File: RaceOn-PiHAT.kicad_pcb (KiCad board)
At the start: 2 copper layers, 65 x 56.5 mm, 76 parts, among them IC1 MIC29302WU, IC10 SN74LVC2G07, IC2 NCP5901B, IC3 NCP5901B, IC4 BD48K60G, IC5 LMR14030, IC6 MPU-9250, IC7 SN74LVC2G07, IC8 SN74LVC2G07, IC9 SN74LVC2G07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

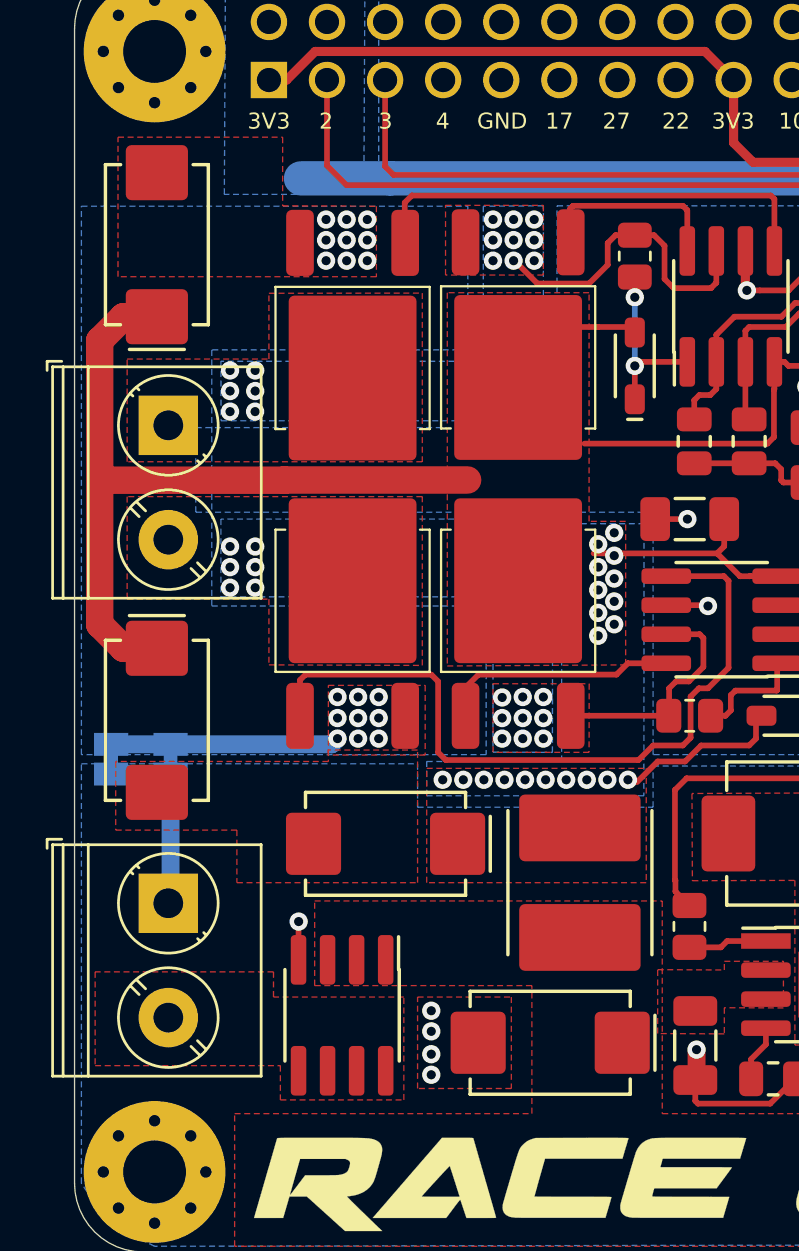
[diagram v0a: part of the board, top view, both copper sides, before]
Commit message: Remove EMI filter, replace low ESR caps with ceramic
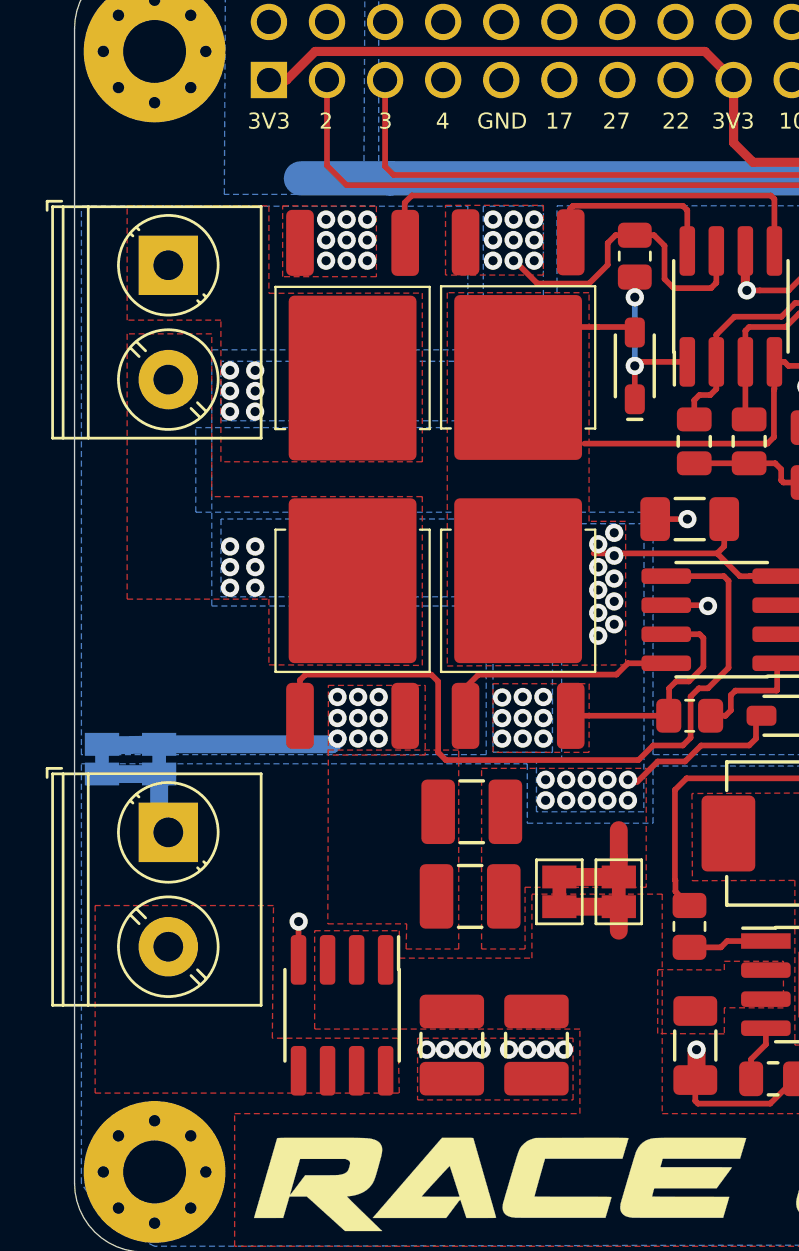
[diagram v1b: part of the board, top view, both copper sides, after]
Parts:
- removed L2: 1uH, Race On:INDM600X600X450L155X490M
- added JP5: SolderJumper_2_Bridged, Jumper:SolderJumper-2_P1.3mm_Bridged_Pad1.0x1.5mm, B.Cu at (120.7, 96.7)
- added JP6: SolderJumper_2_Bridged, Jumper:SolderJumper-2_P1.3mm_Bridged_Pad1.0x1.5mm, B.Cu at (118.2, 96.7)
- C11, C14, C16, C5: value 220uF -> 47uF; footprint Race On:CAPPM730X435X310L135X240L -> Race On:CAPC320X250X270L60M
- JP3, JP4: moved to F.Cu
- moved C14 37.3 mm to (133.5, 109.2)
- moved JP3 22.9 mm to (140.8, 102.5)
- moved C16 21.8 mm to (137.2, 109.2), turned to 90 degrees
- moved JP4 18.0 mm to (138.2, 102.5)
- moved C5 10.7 mm to (134.4, 99.0), turned to 0 degrees
- moved J4 7.00 mm to (121.1, 75.1)
- moved C11 4.36 mm to (134.3, 102.7), turned to 0 degrees
- moved J1 3.10 mm to (121.1, 99.9)
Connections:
- C11 pad 1: +VSW -> -VSW
- C11 pad 2: -VSW -> +VSW
- C14 pad 1: +VSW -> GND
- C14 pad 2: -VSW -> +BATT
- C16 pad 1: +VSW -> GND
- C16 pad 2: -VSW -> +BATT
- C5 pad 1: +BATT -> -VSW
- C5 pad 2: GND -> +VSW
- JP3 pad 1: GND -> +BATT
- JP3 pad 2: -VSW -> +VSW
- JP4 pad 1: GND -> +BATT
- JP4 pad 2: -VSW -> +VSW
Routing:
- net +VSW: track 68.9 -> 39.2 mm
- net +BATT: track 39.1 -> 42.8 mm
- net GND: track 72.4 -> 69.0 mm, vias 40 -> 44

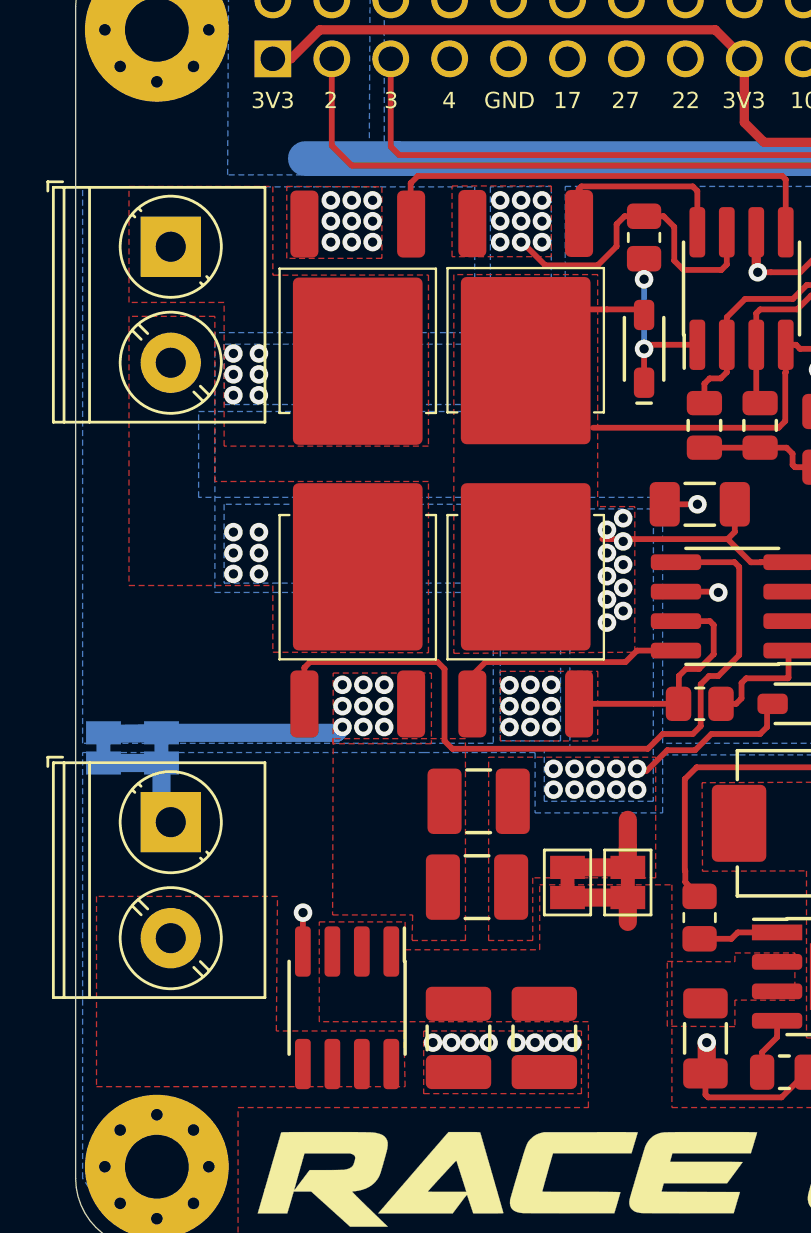
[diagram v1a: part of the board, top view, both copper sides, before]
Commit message: Labeled motor and battery connectors
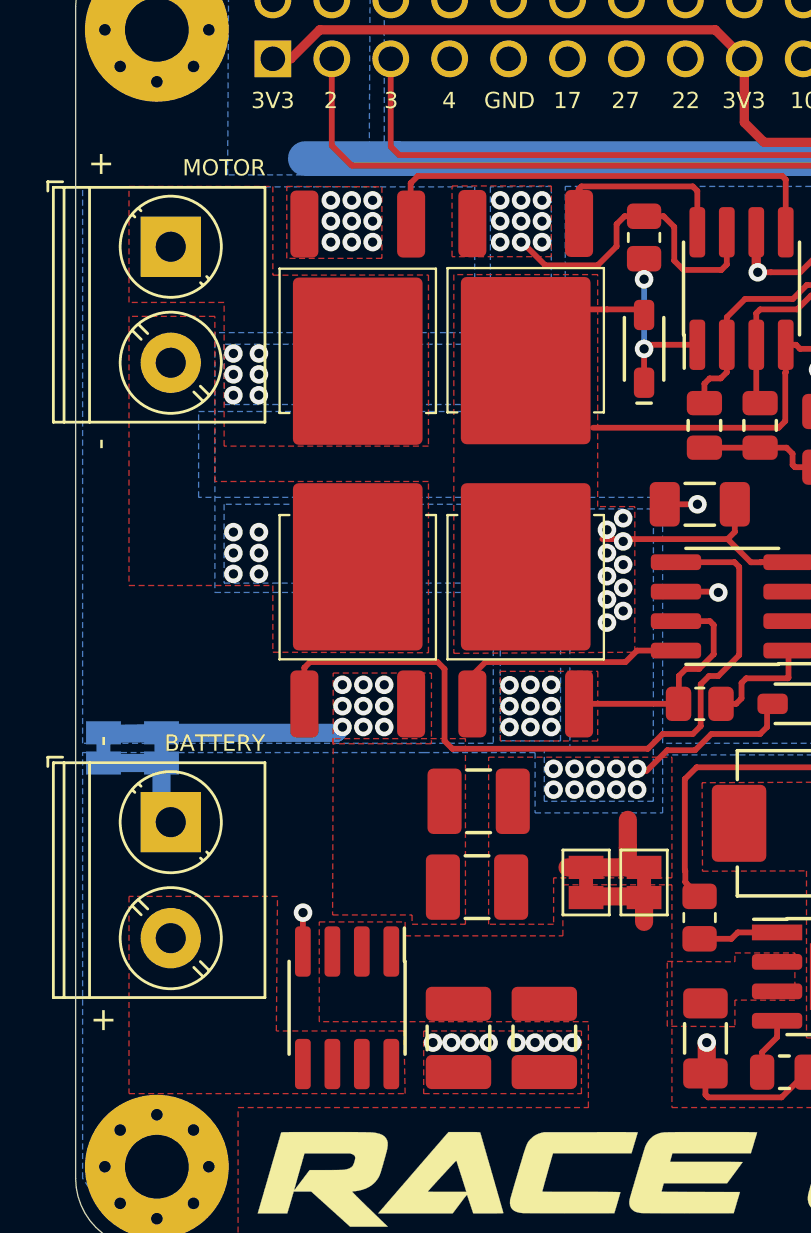
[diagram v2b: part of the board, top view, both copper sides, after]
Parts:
- moved JP4 0.80 mm to (139.0, 102.5)
- moved JP3 0.70 mm to (141.5, 102.5)
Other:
- board text added: "BATTERY"
- board text added: "MOTOR"
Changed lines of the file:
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@@
   (general
     (thickness 1.6)
-    (drawings 72)
+    (drawings 78)
     (tracks 831)
     (zones 0)
@@
   )
   (setup
-    (last_trace_width 0.783)
+    (last_trace_width 0.25)
     (user_trace_width 0.4)
     (user_trace_width 0.783)
@@
   )
   (module Jumper:SolderJumper-2_P1.3mm_Bridged_Pad1.0x1.5mm (layer F.Cu)
-    (at 140.8 102.5 90)
+    (at 141.5 102.5 90)
     (descr "SMD Solder Jumper, 1x1.5mm Pads, 0.3mm gap, bridged with 1 copper strip")
     (tags "solder jumper open")
@@
   )
   (module Jumper:SolderJumper-2_P1.3mm_Bridged_Pad1.0x1.5mm (layer F.Cu)
-    (at 138.2 102.5 90)
+    (at 139 102.5 90)
     (descr "SMD Solder Jumper, 1x1.5mm Pads, 0.3mm gap, bridged with 1 copper strip")
     (tags "solder jumper open")
@@
     )
   )
+  (gr_text BATTERY (at 123 96.5) (layer F.SilkS)
+    (effects (font (size 0.7 0.7) (thickness 0.12)))
+  )
+  (gr_text MOTOR (at 123.4 71.7) (layer F.SilkS)
+    (effects (font (size 0.7 0.7) (thickness 0.12)))
+  )
+  (gr_text - (at 118.2 83.6 270) (layer F.SilkS)
+    (effects (font (size 1 1) (thickness 0.25)))
+  )
+  (gr_text - (at 118.3 96.4 270) (layer F.SilkS)
+    (effects (font (size 1 1) (thickness 0.25)))
+  )
+  (gr_text + (at 118.1 71.5) (layer F.SilkS)
+    (effects (font (size 1 1) (thickness 0.25)))
+  )
+  (gr_text + (at 118.2 108.4) (layer F.SilkS)
+    (effects (font (size 1 1) (thickness 0.25)))
+  )
   (gr_text INT (at 175.6 83.5) (layer F.SilkS)
     (effects (font (size 0.7 0.7) (thickness 0.12)))
@@
   (segment (start 170.438572 93.64849) (end 164.50151 93.64849) (width 0.783) (layer F.Cu) (net 4))
   (segment (start 171.24545 94.455368) (end 170.438572 93.64849) (width 0.783) (layer F.Cu) (net 4))
-  (segment (start 138.2 103.15) (end 140.8 103.15) (width 0.783) (layer F.Cu) (net 4))
-  (segment (start 140.8 103.15) (end 140.8 104.2) (width 0.783) (layer F.Cu) (net 4))
+  (segment (start 139 103.1) (end 141.6 103.1) (width 0.783) (layer F.Cu) (net 4))
+  (segment (start 141.5 103.15) (end 141.5 104.2) (width 0.783) (layer F.Cu) (net 4))
   (segment (start 175.25 99.89) (end 175.24 99.9) (width 0.4) (layer F.Cu) (net 5))
   (segment (start 175.25 97.36) (end 175.25 99.89) (width 0.4) (layer F.Cu) (net 5))
@@
         (xy 142.7 112.2) (xy 164 112.2) (xy 164 118) (xy 124 118) (xy 124 112.2)
         (xy 139.1 112.2) (xy 139.1 108.5) (xy 127.5 108.5) (xy 127.5 104.2) (xy 131.2 104.2)
-        (xy 131.2 105.4) (xy 137 105.4) (xy 137 102.6) (xy 142.7 102.6)
+        (xy 131.2 104.8) (xy 138 104.8) (xy 138 102.6) (xy 142.7 102.6)
       )
     )
@@
     (polygon
       (pts
-        (xy 117.9 111.3) (xy 131.2 111.3) (xy 131.15 108.9) (xy 125.65 108.9) (xy 125.7 103.1)
-        (xy 117.9 103.1)
+        (xy 119.3 111.6) (xy 131.2 111.6) (xy 131.15 108.9) (xy 125.65 108.9) (xy 125.7 103.1)
+        (xy 119.3 103.1)
       )
     )
@@
     (polygon
       (pts
-        (xy 142 102.3) (xy 136.7 102.3) (xy 136.7 105) (xy 134.8 105) (xy 134.8 97.1)
-        (xy 142 97.1)
+        (xy 142.7 102.3) (xy 137.6 102.3) (xy 137.6 104.3) (xy 134.8 104.3) (xy 134.8 97.1)
+        (xy 142.7 97.1)
       )
     )
@@
     (polygon
       (pts
-        (xy 128.075 103.9) (xy 131.525 103.9) (xy 131.5 105) (xy 133.8 105) (xy 133.8 96.3)
+        (xy 128.075 103.9) (xy 131.5 103.9) (xy 131.5 104.3) (xy 133.8 104.3) (xy 133.8 96.3)
         (xy 128.1 96.3)
       )

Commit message: Finished board
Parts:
- added FID1: Fiducial, Race On:FID1M3, F.Cu at (123.5, 91.8)
- IC5: footprint Race On:SOIC9P127_490X600X170L83X41T287X202M -> Race On:SOIC9P127_490X600X170L83X41T287X202
- moved C16 3.10 mm to (140.3, 109.2)
- moved C14 3.10 mm to (136.6, 109.2)
- moved C13 0.60 mm to (143.5, 109.2)
- moved C7 0.40 mm to (155.3, 110.0)
- moved R8 0.40 mm to (157.9, 110.0)
- moved IC5 0.36 mm to (149.3, 106.6)
- moved R10 0.20 mm to (151.5, 110.7)
- moved R9 0.20 mm to (147.3, 110.7)
- moved JP3 0.10 mm to (141.4, 102.5)
- moved JP4 0.10 mm to (138.9, 102.5)
- moved C12 0.09 mm to (143.8, 104.0)
- moved C15 0.07 mm to (155.5, 105.3)
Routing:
- net +BATT: track 42.8 -> 80.1 mm
- net VFB: track 8.43 -> 9.03 mm
- net GND: track 69.0 -> 69.3 mm, vias 44 -> 46
